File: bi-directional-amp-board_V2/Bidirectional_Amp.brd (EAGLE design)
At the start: 78.5 x 52 mm, 106 parts, among them J1 142-0701-851_ALT, J2 142-0701-851_ALT, J3 142-0701-851_ALT, J4 142-0701-851_ALT, J6 142-0701-851_ALT, J7 142-0701-851_ALT, U1 SN74LVC1G32DBVR, U10 TQP9111, U11 SN74LV1T34DBVR, U2 LTC6994-1, U3 LTC6994-1, U4 TQP3M903X, U5 TQP3M903X, U7 QPC1022, U8 QPC1022, U9 SN74LV1T34DBVR

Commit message: V2 version of board after design review, also adds block diagram
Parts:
- removed C13, C36, C40: 100p, oresat-rcl:.0402-B-NOSILK
- added JP4: (no value), pinhead:1X03
- added R29: 10k, oresat-rcl:.0402-B-NOSILK
- added U12: SN74LVC1G32DBVR, SN74LVC1G32DBVR:DBV5
- added U6: SN74LV1T34DBVR, SamacSys_Parts:SOT95P280X145-5N
- C15, C16, C17, C18, C19: device rcl:C0603 -> oresat-rcl:.0402-B-NOSILK
- C5, C7: value 100p -> 100n
- R10, R13, R19, R6, R7, R8, R9: device rcl:R0603 -> oresat-rcl:.0402-B-NOSILK
- R32, R36: value 620 -> 1k
- moved C7 470.7 mm to (-13.5, -442.0), turned to 0 degrees
- moved C5 463.1 mm to (-5.00, -436.5), turned to 0 degrees
- moved R10 381.5 mm to (-0.50, -423.2)
- moved R9 373.8 mm to (-0.50, -410.6)
- moved R7 358.4 mm to (-0.50, -385.1)
- moved R13 351.1 mm to (-0.50, -397.9)
- moved R6 350.7 mm to (-0.50, -372.4)
- moved R8 328.0 mm to (-0.50, -359.8)
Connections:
- new net LNA_DISABLE+3.3V: JP4.1, JP4.3, R29.2, U6.2
- new net LNA_DISABLE_+5.0V: U12.2, U6.4
- new net LNA_ON_OFF: U12.4, U4.6, U5.6
- net +5V: now also U12.5, U6.5; no longer C13.1, C36.1, C40.1
- net GND: now also JP4.2, R29.1, U12.3, U6.3; no longer C13.2, C36.2, C40.2
- net PA_ON_LNA_OFF: now also U12.1; no longer U4.6, U5.6
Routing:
- net +5V: track 14.3 -> 11.8 mm
- net N$22: track 1.79 -> 2.79 mm

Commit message: Prepping for Rev.2 layout.
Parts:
- moved C5 457.0 mm to (-76.0, 15.0)
- moved C7 457.0 mm to (-84.5, 9.50)
- moved JP4 457.0 mm to (-81.5, 12.5)
- moved R10 457.0 mm to (-71.5, 28.2)
- moved R29 457.0 mm to (-72.5, 15.0)
- moved U12 457.0 mm to (-82.0, 4.00)
- moved U6 457.0 mm to (-74.0, 22.0)
- moved C3 418.4 mm to (-91.0, 61.5)
- moved R13 418.4 mm to (-91.0, 10.7)
- moved R6 418.4 mm to (-91.0, 36.0)
- moved R7 418.4 mm to (-91.0, 23.4)
- moved R8 418.4 mm to (-91.0, 48.8)
- moved R9 418.4 mm to (-91.0, -2.05)
- moved C1 295.7 mm to (-50.0, -42.9)
- moved C14 295.7 mm to (-50.0, -30.1)
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
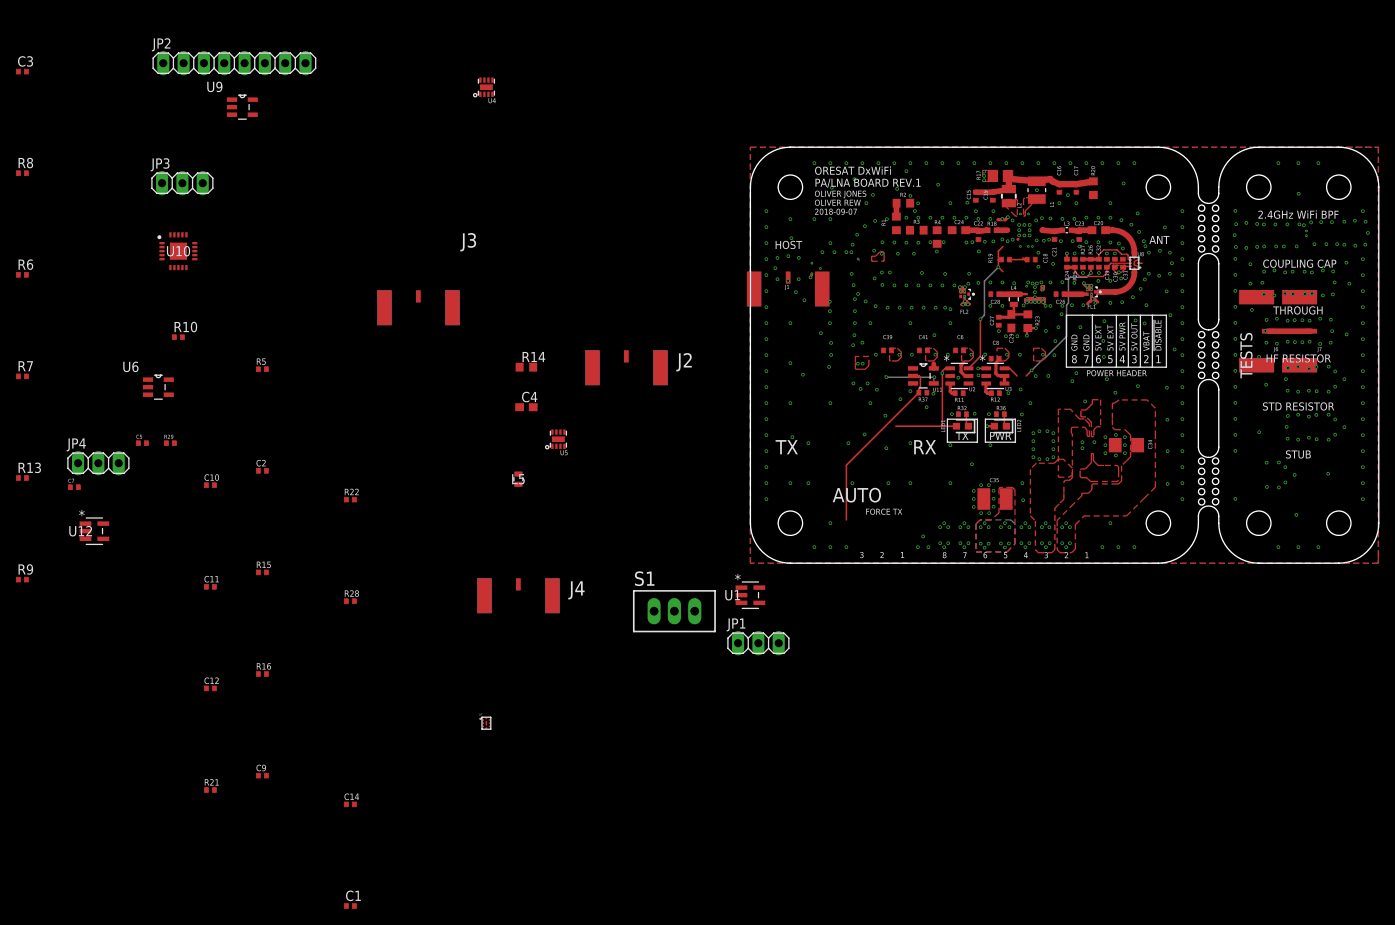
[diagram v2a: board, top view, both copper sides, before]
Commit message: Check in for Vigely to do some modeling. All routed, but not yet polished.
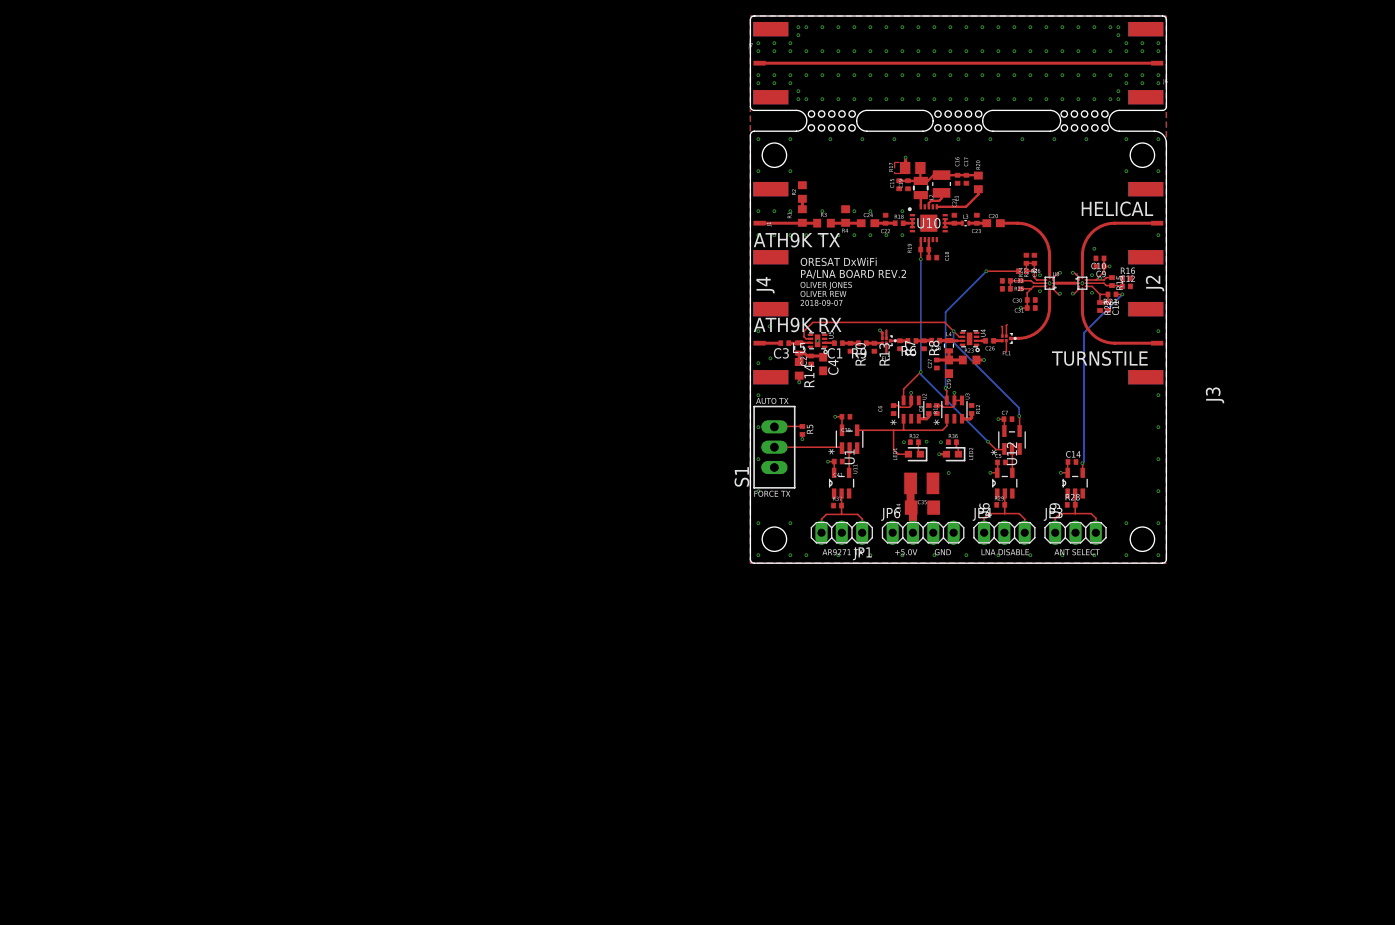
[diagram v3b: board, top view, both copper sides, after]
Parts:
- removed H5, H6, H7, H8: STAND-OFFTIGHT, SparkFun-Hardware:STAND-OFF-TIGHT@1
- removed JP2: (no value), pinhead:1X08
- added JP6: (no value), pinhead:1X04
- moved R21 128.6 mm to (45.2, 33.6), turned to 180 degrees
- moved C12 125.0 mm to (47.0, 34.6)
- moved C9 122.5 mm to (43.7, 37.1), turned to 180 degrees
- moved JP3 119.9 mm to (40.6, 3.81)
- moved R16 118.8 mm to (47.0, 35.6)
- moved C11 117.5 mm to (44.7, 32.1), turned to 270 degrees
- moved C7 117.0 mm to (32.2, 18.0)
- moved U12 115.3 mm to (32.7, 15.4), turned to 90 degrees
- moved C10 114.8 mm to (43.7, 38.1), turned to 180 degrees
- moved R8 114.7 mm to (21.7, 27.3), turned to 270 degrees
- moved U9 114.2 mm to (40.6, 10.0), turned to 90 degrees
- moved JP4 113.6 mm to (31.8, 3.81)
- moved R15 112.2 mm to (45.2, 35.2), turned to 270 degrees
- moved R6 111.5 mm to (20.2, 27.8), turned to 180 degrees
- moved R7 109.8 mm to (18.7, 27.3), turned to 270 degrees
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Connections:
- net N$13 renamed AS-EN
- net N$17 renamed AS-CTRL
- net N$18 renamed HELICAL
- net N$23 renamed TURNSTILE
- net N$32 renamed TXRX-EN
- net N$34 renamed TXRX-CTRL
- net N$47 renamed THROUGH
- removed net AR9271_TX_+5V: U1.1, U11.4
- removed net N$36: C35.1, JP2.3, JP2.4
- removed net N$43: C34.1, JP2.7
- new net N$13: U1.2, U11.4
- net +5V: now also C34.1, C35.1, JP6.1, JP6.2; no longer JP2.5
- net GND: now also JP6.3, JP6.4; no longer JP2.1, JP2.2
- net N$5: now also U1.1; no longer U1.2
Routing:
- net THROUGH: track 5.38 -> 49.7 mm
- net LNA_ON_OFF: track 0.00 -> 38.5 mm, vias 0 -> 2
- net +5V: track 11.8 -> 45.1 mm, vias 22 -> 15
- net ANT_SEL_+5.0V: track 0.00 -> 25.2 mm, vias 0 -> 2
- net PA_ON_LNA_OFF: track 18.2 -> 35.7 mm, vias 2 -> 3
- net GND: track 28.9 -> 13.1 mm, vias 575 -> 195
- net TURNSTILE: track 0.00 -> 13.9 mm
- net HELICAL: track 0.00 -> 13.9 mm
- net ANT_SEL+3.3V: track 0.00 -> 11.7 mm
- net LNA_DISABLE+3.3V: track 0.00 -> 11.6 mm
- net AR9271_TX_+3.3V: track 22.6 -> 11.6 mm
- net N$5: track 0.00 -> 8.50 mm
- net N$2: track 0.00 -> 7.25 mm
- net AR9271_TX_+5V: track 7.04 -> 0.00 mm, vias 2 -> 0
- net N$30: track 0.00 -> 6.49 mm
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- removed copper zone on layer 1, net N$19
- removed copper zone on layer 1, net N$20
- removed copper zone on layer 1, net N$36
- removed copper zone on layer 16, net N$36
- removed copper zone on layer 2, net N$37
- removed copper zone on layer 15, net N$38
- removed copper zone on layer 1, net SWA1
- removed copper zone on layer 1, net SWB1
- removed copper zone on layer 1, net VIN1
- removed copper zone on layer 1, net VOUT1
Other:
- board size 78.5 x 52 mm -> 52 x 68.4 mm
- board text added: "+5.0V"
- board text added: "ANT SELECT"
- board text added: "AR9271 TX"
- board text added: "ATH9K RX"
- board text added: "ATH9K TX"
- board text added: "AUTO TX"
- board text added: "HELICAL"
- board text added: "LNA DISABLE"
- board text added: "ORESAT DxWiFi PA/LNA BOARD REV.2"
- board text added: "TURNSTILE"
- board text removed: "!DISABLE"
- board text removed: "1"
- board text removed: "2"
- board text removed: "2.4GHz WiFi BPF"
- board text removed: "3"
- board text removed: "4"
- board text removed: "5"
- board text removed: "5V EXT"
- board text removed: "5V OUT"
- board text removed: "5V PWR"
- board text removed: "6"
- board text removed: "7"
- board text removed: "8"
- board text removed: "ANT"
- board text removed: "AUTO"
- board text removed: "COUPLING CAP"
- board text removed: "HF RESISTOR"
- board text removed: "HOST"
- board text removed: "ORESAT DxWiFi PA/LNA BOARD REV.1"
- board text removed: "POWER HEADER"
- board text removed: "PWR"
- board text removed: "RX"
- board text removed: "STD RESISTOR"
- board text removed: "STUB"
- board text removed: "TESTS"
- board text removed: "THROUGH"
- board text removed: "TX"
- board text removed: "VBAT"

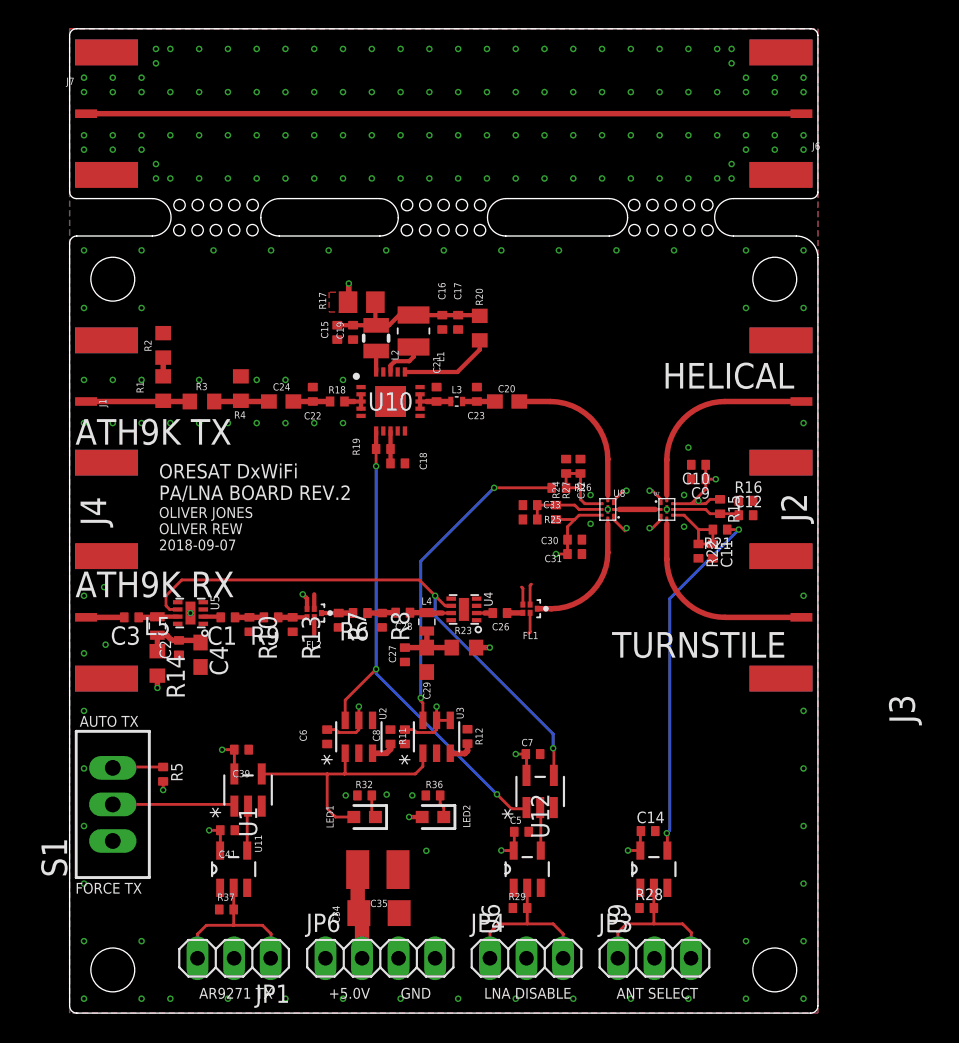
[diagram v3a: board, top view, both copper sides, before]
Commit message: Finished layout! More vias, fixed Vpd issue for LNAs, cleaned up tnames, etc etc.
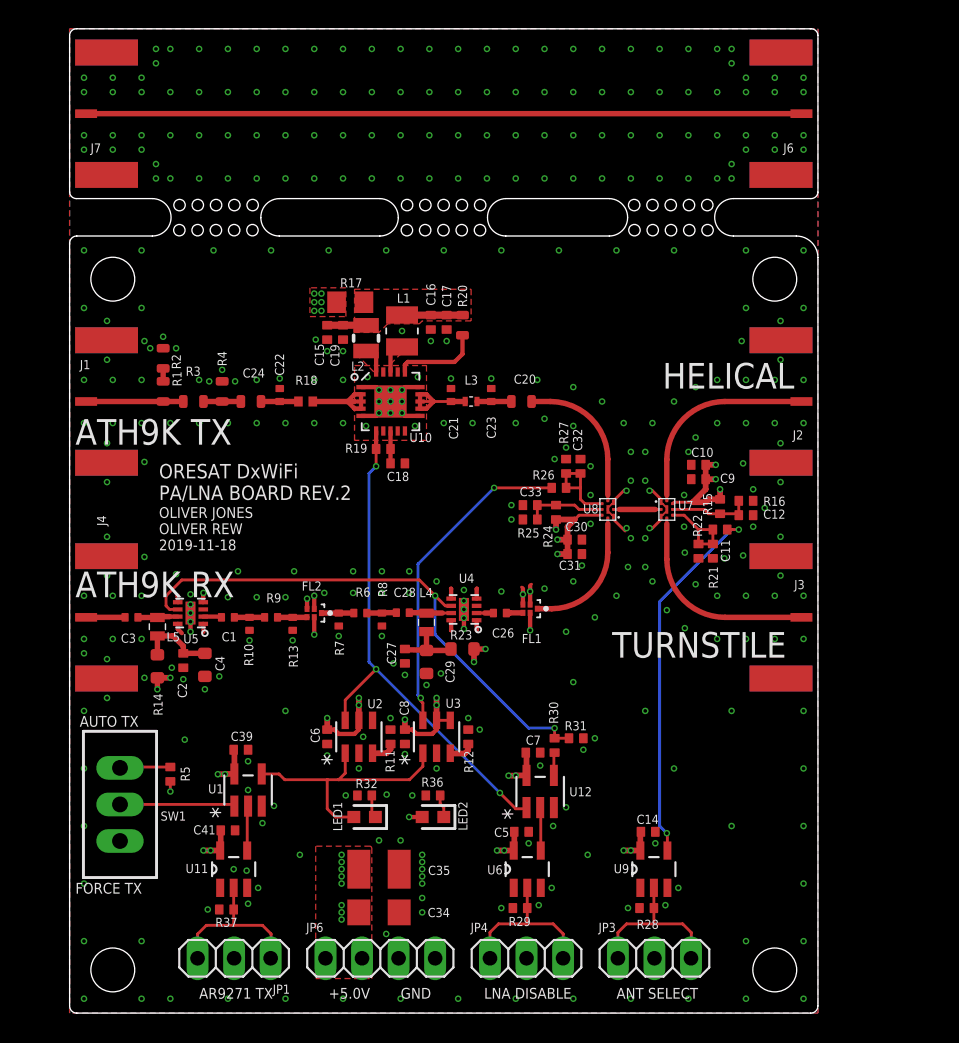
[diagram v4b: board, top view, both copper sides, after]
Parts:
- removed S1: TL36PO, switch:TL3XPO
- added R30: 33k, oresat-rcl:.0402-B-NOSILK
- added R31: 10k, oresat-rcl:.0402-B-NOSILK
- added SW1: TL36PO, switch:TL3XPO
- C1, C21, C22, C23, C26, C28, C3, R10, R13, R6, R7, R8, R9: device oresat-rcl:.0402-B-NOSILK -> oresat-rcl:.0402-C-NOSILK
- C20, C24: device rcl:C0603 -> oresat-rcl:.0603-C-NOSILK
- C29, C4: device rcl:C0603 -> oresat-rcl:.0603-B-NOSILK
- R1, R2, R20, R3, R4: device rcl:R0603 -> oresat-rcl:.0603-C-NOSILK
- R14, R23: device rcl:R0603 -> oresat-rcl:.0603-B-NOSILK
- U10: device SamacSys_Parts:QFN50P400X400X102-21N -> oresat-samacsys_Parts:QFN50P400X400X102-21N
- moved C22 2.30 mm to (14.6, 43.0)
- moved R18 2.20 mm to (16.4, 42.5)
- moved C24 2.10 mm to (12.6, 42.5)
- moved R4 1.32 mm to (10.6, 43.2)
- moved R20 1.22 mm to (27.3, 47.8)
- moved C21 1.00 mm to (26.5, 43.0)
- moved C23 1.00 mm to (29.3, 43.0)
- moved C20 1.00 mm to (31.4, 42.5)
- moved L3 1.00 mm to (27.9, 42.5)
- moved C2 0.95 mm to (7.90, 24.5)
- moved R2 0.90 mm to (6.50, 45.5)
- moved C17 0.80 mm to (26.2, 48.0)
- moved R17 0.80 mm to (19.5, 49.4)
- moved C16 0.80 mm to (25.1, 48.0)
- moved L1 0.80 mm to (23.1, 47.4)
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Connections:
- new net N$17: R30.2, U12.4
- net GND: now also R31.2, SW1.1, U10.1, U10.10, U10.11, U10.15, U10.17, U10.19, U10.5, U10.7, U10.9, U4.1, U4.3, U4.4, U4.5, U4.8, U5.1, U5.3, U5.4, U5.5, U5.8; no longer S1.1
- net LNA_ON_OFF: now also R30.1, R31.1; no longer U12.4
- net N$3: now also SW1.3; no longer S1.3
- net N$5: now also SW1.2; no longer S1.2
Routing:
- net GND: track 13.1 -> 28.2 mm, vias 195 -> 390
- net N$21: track 11.8 -> 6.96 mm
- net N$56: track 2.15 -> 6.66 mm
- net N$24: track 3.14 -> 6.45 mm
- net N$17: track 0.00 -> 1.60 mm
- net +5V: track 45.1 -> 46.6 mm, vias 15 -> 42
- net N$16: track 2.99 -> 1.65 mm
- net PA_PAD_OUT: track 3.84 -> 2.60 mm
- net N$9: track 4.32 -> 5.40 mm
- net N$3: track 3.52 -> 4.38 mm
- net PA_MATCH_OUT: track 10.7 -> 9.86 mm
- net ANT_SEL_+5.0V: track 25.2 -> 25.9 mm
- net N$31: track 1.46 -> 2.10 mm
- net LNA_ON_OFF: track 38.5 -> 38.0 mm
- added copper zone on layer 15, net GND
- added copper zone on layer 1, net N$16
- added copper zone on layer 1, net N$21
- added copper zone on layer 1, net N$31
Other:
- board text added: "OLIVER JONES OLIVER REW 2019-11-18"
- board text removed: "OLIVER JONES OLIVER REW 2018-09-07"

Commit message: Cleanup, suggested by Oliver(s).
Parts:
- moved R17 2.33 mm to (17.2, 49.0)
- moved C19 2.27 mm to (17.3, 45.8), turned to 180 degrees
- moved C6 1.00 mm to (16.9, 19.2)
- moved R11 1.00 mm to (21.3, 19.2)
- moved U2 1.00 mm to (19.1, 19.2)
- moved L2 0.86 mm to (19.9, 46.4), turned to 90 degrees
- moved C15 0.72 mm to (17.3, 46.9), turned to 180 degrees
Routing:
- net N$21: track 6.96 -> 4.20 mm
- net N$31: track 2.10 -> 3.46 mm
- net PA_ON_LNA_OFF: track 35.9 -> 36.9 mm
- net GND: vias 390 -> 394

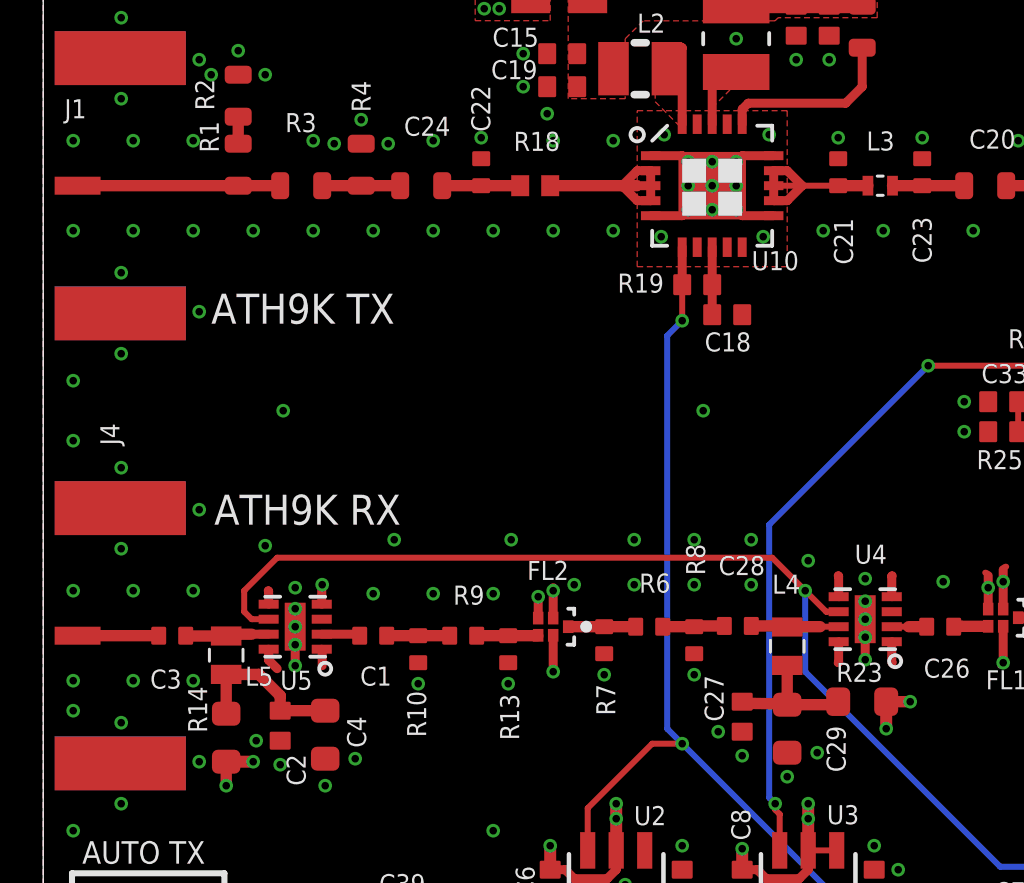
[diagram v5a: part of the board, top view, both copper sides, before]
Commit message: Fixed trace widths a bit. Should be ready to go.
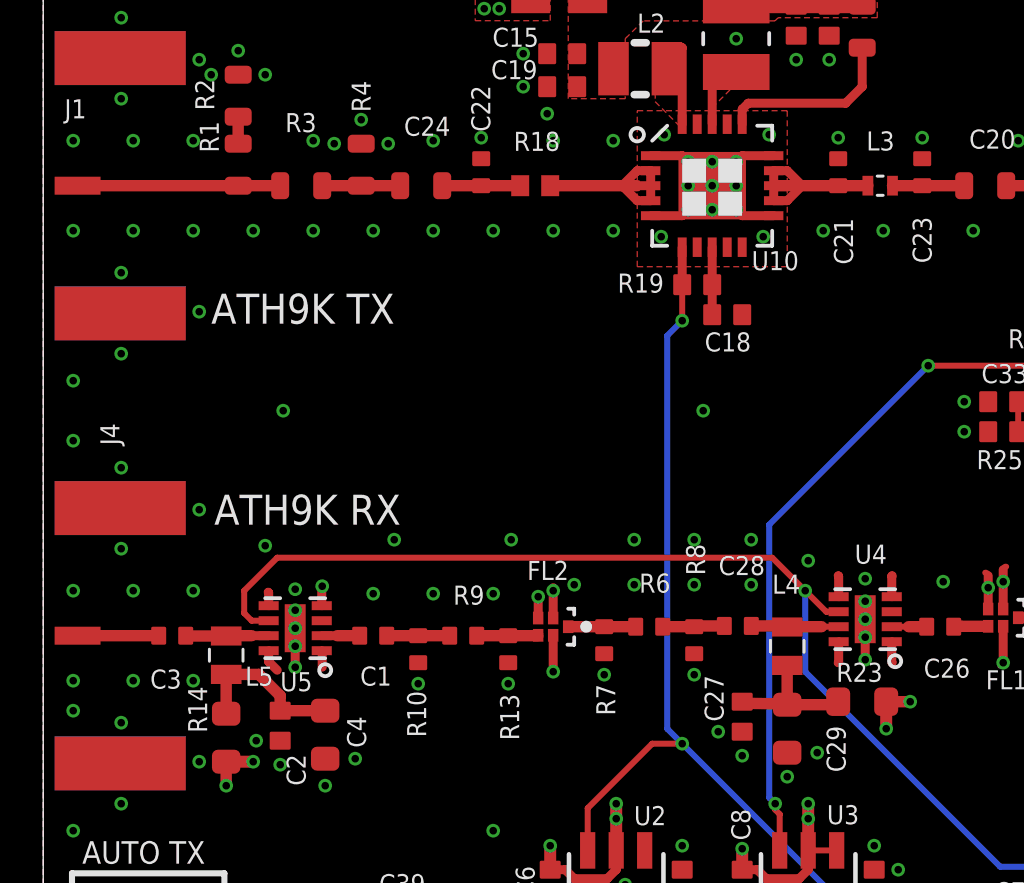
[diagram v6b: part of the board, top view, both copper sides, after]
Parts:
- moved U5 0.05 mm to (8.40, 27.8)

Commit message: Made the LNAs the correct part number.
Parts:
- U4, U5: value TQP3M903X -> TQP3M9037
